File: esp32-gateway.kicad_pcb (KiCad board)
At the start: 2 copper layers, 55 x 95 mm, 43 parts, among them J1 USB_B_Micro, J2 Conn_Coaxial, J3 Ext LED header, J4 Header Left, J5 Header Right, Q1 Q_NPN_BEC, Q2 Q_NPN_BEC, SW1 SW_RESET, SW2 SW_INCLUSION, SW3 SW_GEN1, SW4 SW_BOOT, U1 RFM69HCW, U2 NRF24L01_Breakout, U3 ESP-WROOM-32, U4 RFM69CW, U5 RFM69(H)W, U6 AMS1117-3.3, U7 CH340G, Y1 Crystal 12Mhz

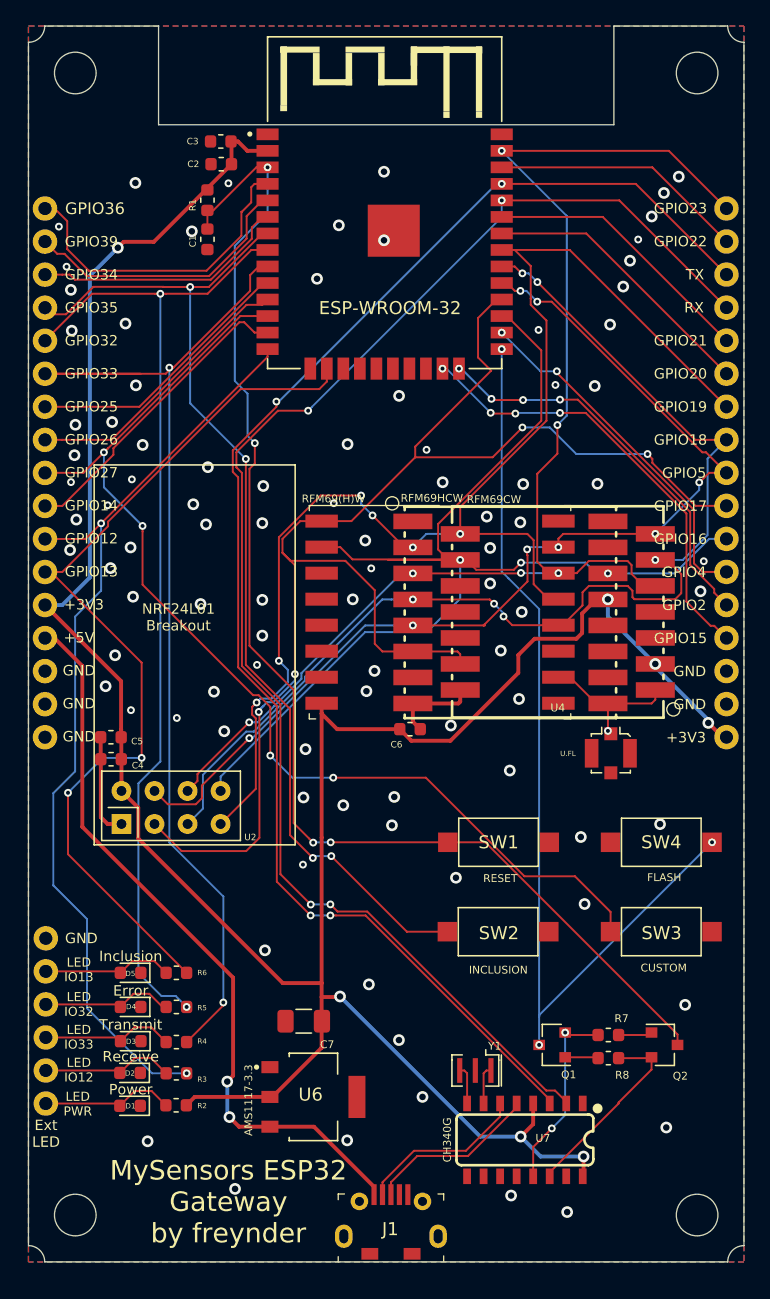
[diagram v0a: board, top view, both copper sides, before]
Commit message: Major redesign.
- Changed headers to XH2.54 connectors for leds and buttons
- Added secondary regulator to power RF modules
- Changed RFM69 footprints to remove unused pads
- Changed CHG340G chip to CHG340C, eliminating the crystal
- Relayed all traces for cleaner design
- Added capacitors at USB input power
- Added second capacitor for decoupling at RFM69 modules
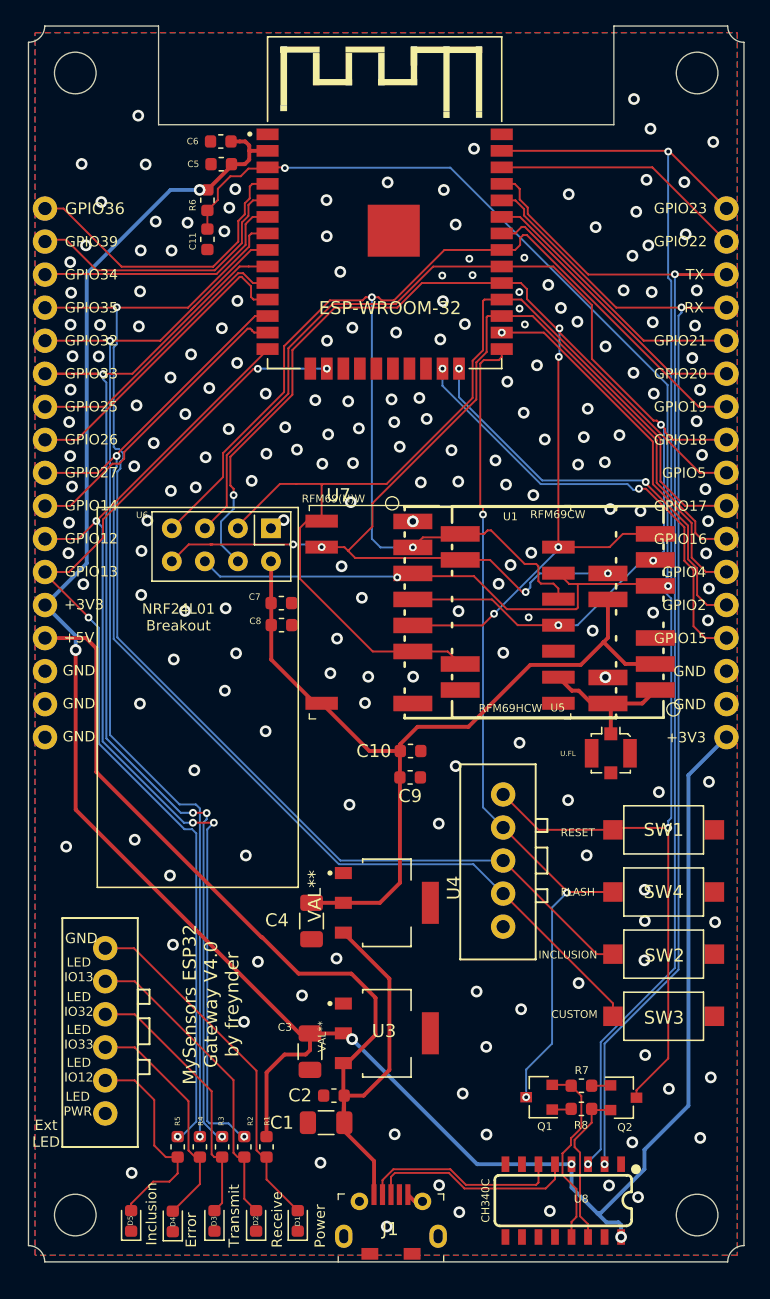
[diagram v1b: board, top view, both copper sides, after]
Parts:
- removed the C6 at (144.3, 119.0)
- removed Y1: Crystal 12Mhz, Crystal:Resonator_SMD_muRata_CSTxExxV-3Pin_3.0x1.1mm
- added C1: 4.7uF, Capacitor_SMD:C_1206_3216Metric, F.Cu at (137.9, 149.3)
- added C10: 10uF, Capacitor_SMD:C_0603_1608Metric, F.Cu at (144.4, 120.7)
- added C2: 0.1uF, Capacitor_SMD:C_0603_1608Metric, F.Cu at (138.5, 147.2)
- added C4: 22uF, Capacitor_SMD:C_1206_3216Metric, F.Cu at (136.8, 133.8)
- added C9: 0.1uF, Capacitor_SMD:C_0603_1608Metric, F.Cu at (144.3, 122.8)
- added J2: Button Connector, custom:connector-XH2.54-01x05, F.Cu at (151.5, 129.2)
- added U4: VAL**, custom:AMS1117-3.3, F.Cu at (142.6, 132.4)
- J3: footprint Sparkfun Connectors:1X06_NO_SILK -> custom:connector-XH2.54-01x06
- U1: footprint Sparkfun RF:RFM69HCW-XXXS2 -> custom:RFM69HCW-XXXS2-MINPADS
- U3: renamed from U6; value AMS1117-3.3 -> VAL**
- U5: renamed from U4; footprint Sparkfun RF:RFM69CW-XXXS2 -> custom:RFM69CW-XXXS2-MINPADS
- U7: renamed from U5; footprint RF_Module:HOPERF_RFM69HW -> custom:HOPERF_RFM69HW-MINPADS
- U8: renamed from U7; value CH340G -> CH340C
- moved U6 25.5 mm to (133.6, 103.6), turned to 270 degrees
- moved D5 19.1 mm to (122.9, 156.8), turned to 90 degrees
- moved C7 17.8 mm to (134.4, 109.4), turned to 180 degrees
- moved D4 16.8 mm to (126.1, 156.9), turned to 90 degrees
- moved C8 15.7 mm to (134.4, 111.0), turned to 180 degrees
- moved D1 15.6 mm to (135.7, 156.8), turned to 90 degrees
- moved D3 15.2 mm to (129.3, 156.8), turned to 90 degrees
- moved D2 14.9 mm to (132.5, 156.8), turned to 90 degrees
- moved R5 13.4 mm to (126.5, 151.2), turned to 90 degrees
- moved SW2 12.8 mm to (163.8, 136.3)
- moved SW1 12.7 mm to (163.8, 126.8)
- moved R4 10.9 mm to (128.2, 151.2), turned to 90 degrees
- moved R3 8.79 mm to (129.9, 151.2), turned to 90 degrees
- moved J3 8.24 mm to (120.9, 141.0), turned to 270 degrees
- moved R2 7.70 mm to (131.6, 151.2), turned to 90 degrees
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- renumbered C1 to C11, C7 to C3, C2 to C5, C3 to C6, C4 to C7, C5 to C8, J2 to J4, J4 to J5, J5 to J6, R2 to R1, R3 to R2, R4 to R3, R5 to R4, R6 to R5, R1 to R6, U3 to U2, U2 to U6
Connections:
- C3 pad 1: +3V3 -> LEDB
- C5 pad 1: +3V3 -> LEDB
- C6 pad 1: +3V3 -> LEDB
- C7 pad 2: +3V3 -> RFPOW
- C8 pad 2: +3V3 -> RFPOW
- J1 pad 4: Net-(J1-Pad4) -> (no net)
- J5 pad 13: +3V3 -> LEDB
- J6 pad 1: +3V3 -> LEDB
- R1 pad 2: +3V3 -> LEDB
- R6 pad 1: +3V3 -> LEDB
- U1 pad 11: Net-(U1-Pad11) -> (no net)
- U1 pad 12: Net-(U1-Pad12) -> (no net)
- U1 pad 13: +3V3 -> RFPOW
- U1 pad 15: Net-(U1-Pad15) -> (no net)
- U1 pad 16: Net-(U1-Pad16) -> (no net)
- U1 pad 7: Net-(U1-Pad7) -> (no net)
- U2 pad 17: Net-(U3-Pad17) -> (no net)
- U2 pad 18: Net-(U3-Pad18) -> (no net)
- U2 pad 19: Net-(U3-Pad19) -> (no net)
- U2 pad 2: +3V3 -> LEDB
- U2 pad 20: Net-(U3-Pad20) -> (no net)
- U2 pad 21: Net-(U3-Pad21) -> (no net)
- U2 pad 22: Net-(U3-Pad22) -> (no net)
- U3 pad 2: +3V3 -> LEDB
- U5 pad 10: Net-(U4-Pad10) -> (no net)
- U5 pad 11: Net-(U4-Pad11) -> (no net)
- U5 pad 12: Net-(U4-Pad12) -> (no net)
- U5 pad 2: +3V3 -> RFPOW
- U5 pad 4: Net-(U4-Pad4) -> (no net)
- U6 pad 2: +3V3 -> RFPOW
- U7 pad 3: Net-(U5-Pad3) -> (no net)
- U7 pad 4: Net-(U5-Pad4) -> (no net)
- U7 pad 5: Net-(U5-Pad5) -> (no net)
- U7 pad 6: Net-(U5-Pad6) -> (no net)
- U7 pad 7: Net-(U5-Pad7) -> (no net)
- U7 pad 8: +3V3 -> RFPOW
- U8 pad 10: Net-(U7-Pad10) -> (no net)
- U8 pad 11: Net-(U7-Pad11) -> (no net)
- U8 pad 12: Net-(U7-Pad12) -> (no net)
- U8 pad 15: Net-(U7-Pad15) -> (no net)
- U8 pad 16: +3V3 -> LEDB
- U8 pad 4: +3V3 -> LEDB
- U8 pad 7: XI -> (no net)
- U8 pad 8: XO -> (no net)
- U8 pad 9: Net-(U7-Pad9) -> (no net)
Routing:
- net +3V3: track 199.2 -> 0.00 mm, vias 7 -> 0
- net LEDB: track 0.00 -> 172.0 mm, vias 0 -> 5
- net RFPOW: track 0.00 -> 65.5 mm
- net CE-RST: track 110.9 -> 81.0 mm, vias 4 -> 0
- net +5V: track 57.4 -> 78.2 mm, vias 2 -> 0
- net ESPRX: track 113.1 -> 92.8 mm, vias 4 -> 2
- net IO5: track 81.2 -> 100.3 mm, vias 8 -> 5
- net EN: track 98.2 -> 115.9 mm, vias 4 -> 2
- net Net-(D1-Pad2): track 10.2 -> 27.7 mm
- net ESPTX: track 112.3 -> 96.1 mm, vias 4 -> 2
- net IO35: track 80.5 -> 94.3 mm, vias 4 -> 1
- net Net-(D2-Pad2): track 10.3 -> 24.1 mm
- net GND: track 14.8 -> 2.58 mm, vias 94 -> 196
- net Net-(D3-Pad2): track 10.3 -> 20.7 mm
- net IO23: track 100.8 -> 91.6 mm, vias 6 -> 3
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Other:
- net class ANT added: clearance 0.127, trace_width 0.3048, via_dia 0.6, via_drill 0.3
- board text added: "MySensors ESP32 Gateway V4.0 by freynder"
- board text removed: "MySensors ESP32 Gateway by freynder"

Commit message: Silkscreen optimization plus BOM
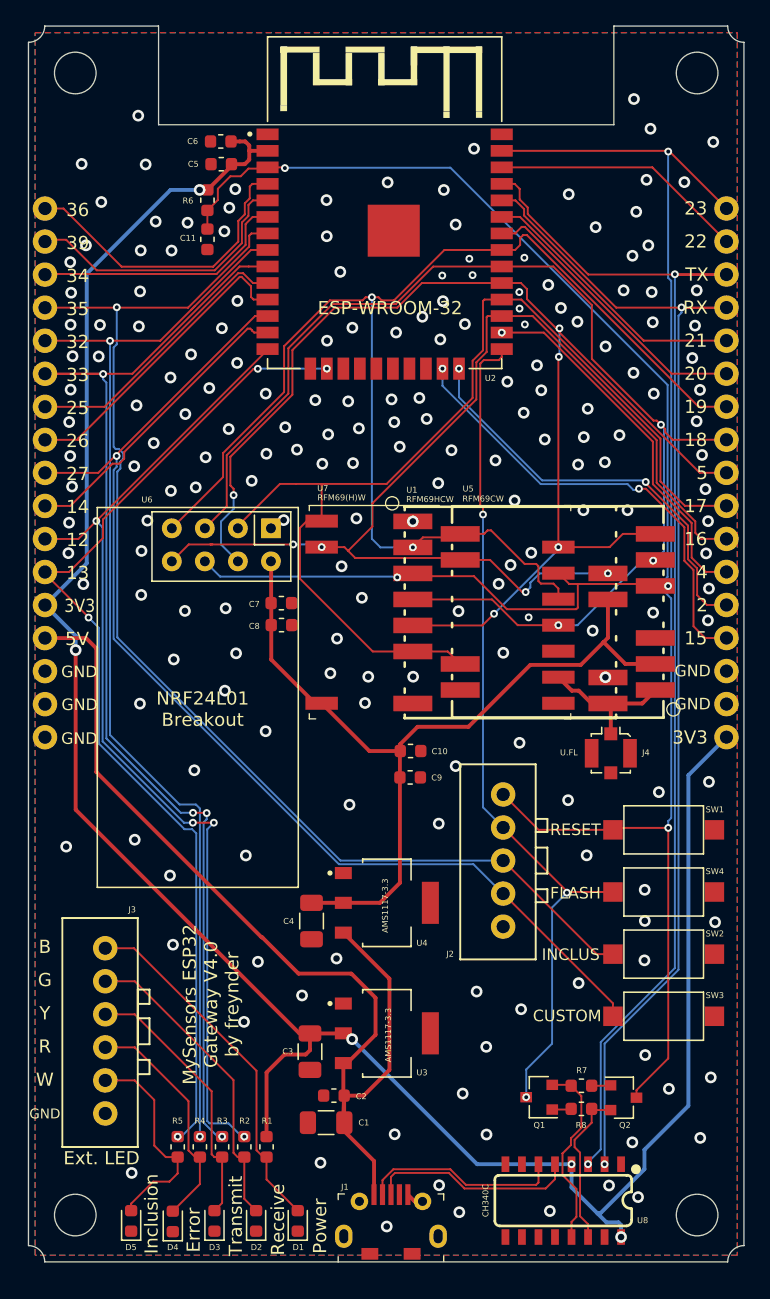
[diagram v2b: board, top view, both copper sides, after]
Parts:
- added REF**: OSHW-Logo2_24.3x20mm_SilkScreen, Symbol:OSHW-Logo2_24.3x20mm_SilkScreen, B.Cu at (141.1, 133.8)
- U3, U4: value VAL** -> AMS1117-3.3
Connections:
- J1 pad 4: (no net) -> Net-(J1-Pad4)
- U1 pad 11: (no net) -> Net-(U1-Pad11)
- U1 pad 12: (no net) -> Net-(U1-Pad12)
- U1 pad 15: (no net) -> Net-(U1-Pad15)
- U1 pad 16: (no net) -> Net-(U1-Pad16)
- U1 pad 7: (no net) -> Net-(U1-Pad7)
- U2 pad 17: (no net) -> Net-(U2-Pad17)
- U2 pad 18: (no net) -> Net-(U2-Pad18)
- U2 pad 19: (no net) -> Net-(U2-Pad19)
- U2 pad 20: (no net) -> Net-(U2-Pad20)
- U2 pad 21: (no net) -> Net-(U2-Pad21)
- U2 pad 22: (no net) -> Net-(U2-Pad22)
- U5 pad 10: (no net) -> Net-(U5-Pad10)
- U5 pad 11: (no net) -> Net-(U5-Pad11)
- U5 pad 12: (no net) -> Net-(U5-Pad12)
- U5 pad 4: (no net) -> Net-(U5-Pad4)
- U7 pad 3: (no net) -> Net-(U7-Pad3)
- U7 pad 4: (no net) -> Net-(U7-Pad4)
- U7 pad 5: (no net) -> Net-(U7-Pad5)
- U7 pad 6: (no net) -> Net-(U7-Pad6)
- U7 pad 7: (no net) -> Net-(U7-Pad7)
- U8 pad 10: (no net) -> Net-(U8-Pad10)
- U8 pad 11: (no net) -> Net-(U8-Pad11)
- U8 pad 12: (no net) -> Net-(U8-Pad12)
- U8 pad 15: (no net) -> Net-(U8-Pad15)
- U8 pad 7: (no net) -> Net-(U8-Pad7)
- U8 pad 8: (no net) -> Net-(U8-Pad8)
- U8 pad 9: (no net) -> Net-(U8-Pad9)
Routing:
- net GND: vias 196 -> 195
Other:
- board text added: "12"
- board text added: "13"
- board text added: "14"
- board text added: "15"
- board text added: "16"
- board text added: "17"
- board text added: "18"
- board text added: "19"
- board text added: "2"
- board text added: "20"
- board text added: "21"
- board text added: "22"
- board text added: "23"
- board text added: "25"
- board text added: "26"
- board text added: "27"
- board text added: "32"
- board text added: "33"
- board text added: "34"
- board text added: "35"
- board text added: "36"
- board text added: "39"
- board text added: "3V3"
- board text added: "4"
- board text added: "5"
- board text added: "5V"
- board text added: "B"
- board text added: "Ext. LED"
- board text added: "G"
- board text added: "INCLUS"
- board text added: "R"
- board text added: "W"
- board text added: "Y"
- board text removed: "+3V3"
- board text removed: "+5V"
- board text removed: "Ext LED"
- board text removed: "GPIO12"
- board text removed: "GPIO13"
- board text removed: "GPIO14"
- board text removed: "GPIO15"
- board text removed: "GPIO16"
- board text removed: "GPIO17"
- board text removed: "GPIO18"
- board text removed: "GPIO19"
- board text removed: "GPIO2"
- board text removed: "GPIO20"
- board text removed: "GPIO21"
- board text removed: "GPIO22"
- board text removed: "GPIO23"
- board text removed: "GPIO25"
- board text removed: "GPIO26"
- board text removed: "GPIO27"
- board text removed: "GPIO32"
- board text removed: "GPIO33"
- board text removed: "GPIO34"
- board text removed: "GPIO35"
- board text removed: "GPIO36"
- board text removed: "GPIO39"
- board text removed: "GPIO4"
- board text removed: "GPIO5"
- board text removed: "INCLUSION"
- board text removed: "LED IO12"
- board text removed: "LED IO13"
- board text removed: "LED IO32"
- board text removed: "LED IO33"
- board text removed: "LED PWR"

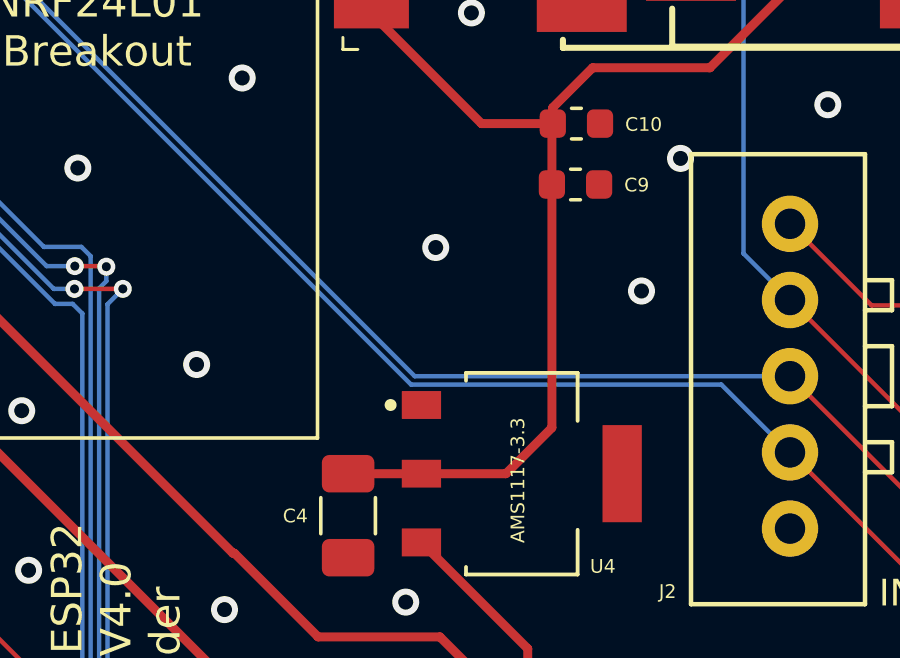
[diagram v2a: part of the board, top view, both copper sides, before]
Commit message: Fixed power routing error
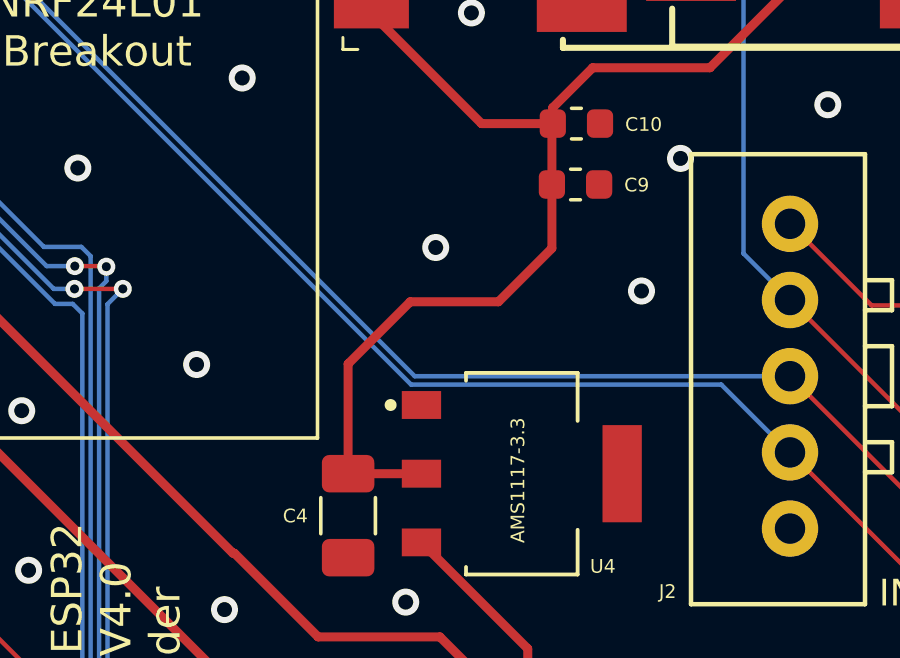
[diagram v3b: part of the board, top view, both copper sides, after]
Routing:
- net RFPOW: track 65.5 -> 66.6 mm
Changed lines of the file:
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@@
     (thickness 1.6)
     (drawings 108)
-    (tracks 884)
+    (tracks 886)
     (zones 0)
     (modules 49)
@@
     (pcbplotparams
       (layerselection 0x010fc_ffffffff)
-      (usegerberextensions true)
+      (usegerberextensions false)
       (usegerberattributes false)
       (usegerberadvancedattributes false)
@@
       (drillshape 0)
       (scaleselection 1)
-      (outputdirectory "gerber_protel"))
+      (outputdirectory "gerber"))
   )
   (net 0 "")
@@
   (segment (start 131.975 74.185) (end 131.663299 73.873299) (width 0.3) (layer F.Cu) (net 43))
   (segment (start 136.76 132.4) (end 139.205 132.4) (width 0.3) (layer F.Cu) (net 44) (status 30))
-  (segment (start 143.5525 130.8675) (end 143.5525 122.76) (width 0.3) (layer F.Cu) (net 44) (status 20))
-  (segment (start 142.02 132.4) (end 143.5525 130.8675) (width 0.3) (layer F.Cu) (net 44))
   (segment (start 143.5525 120.76) (end 143.5825 120.73) (width 0.3) (layer F.Cu) (net 44) (status 30))
   (segment (start 143.5525 122.76) (end 143.5525 120.76) (width 0.3) (layer F.Cu) (net 44) (status 30))
@@
   (segment (start 133.6525 106.1625) (end 133.64 106.15) (width 0.3) (layer F.Cu) (net 44) (status 30))
   (segment (start 133.6525 109.36) (end 133.6525 106.1625) (width 0.3) (layer F.Cu) (net 44) (status 30))
-  (segment (start 139.205 132.4) (end 142.02 132.4) (width 0.3) (layer F.Cu) (net 44) (status 10))
+  (segment (start 136.76 132.4) (end 136.76 128.74) (width 0.3) (layer F.Cu) (net 44))
+  (segment (start 136.76 128.74) (end 138.83 126.67) (width 0.3) (layer F.Cu) (net 44))
+  (segment (start 138.83 126.67) (end 141.77 126.67) (width 0.3) (layer F.Cu) (net 44))
+  (segment (start 143.5525 124.8875) (end 143.5525 122.76) (width 0.3) (layer F.Cu) (net 44))
+  (segment (start 141.77 126.67) (end 143.5525 124.8875) (width 0.3) (layer F.Cu) (net 44))
   (zone (net 1) (net_name GND) (layer F.Cu) (hatch edge 0.508)
     (connect_pads (clearance 0.15))
